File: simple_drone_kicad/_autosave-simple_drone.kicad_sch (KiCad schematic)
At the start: 35 parts, among them P1 USB_C_Plug_USB2.0, Q1 FDN340P, U1 BMI088, U2 BMP581, U3 FT260S-U, U4 LMV358, Y1 Crystal_GND23

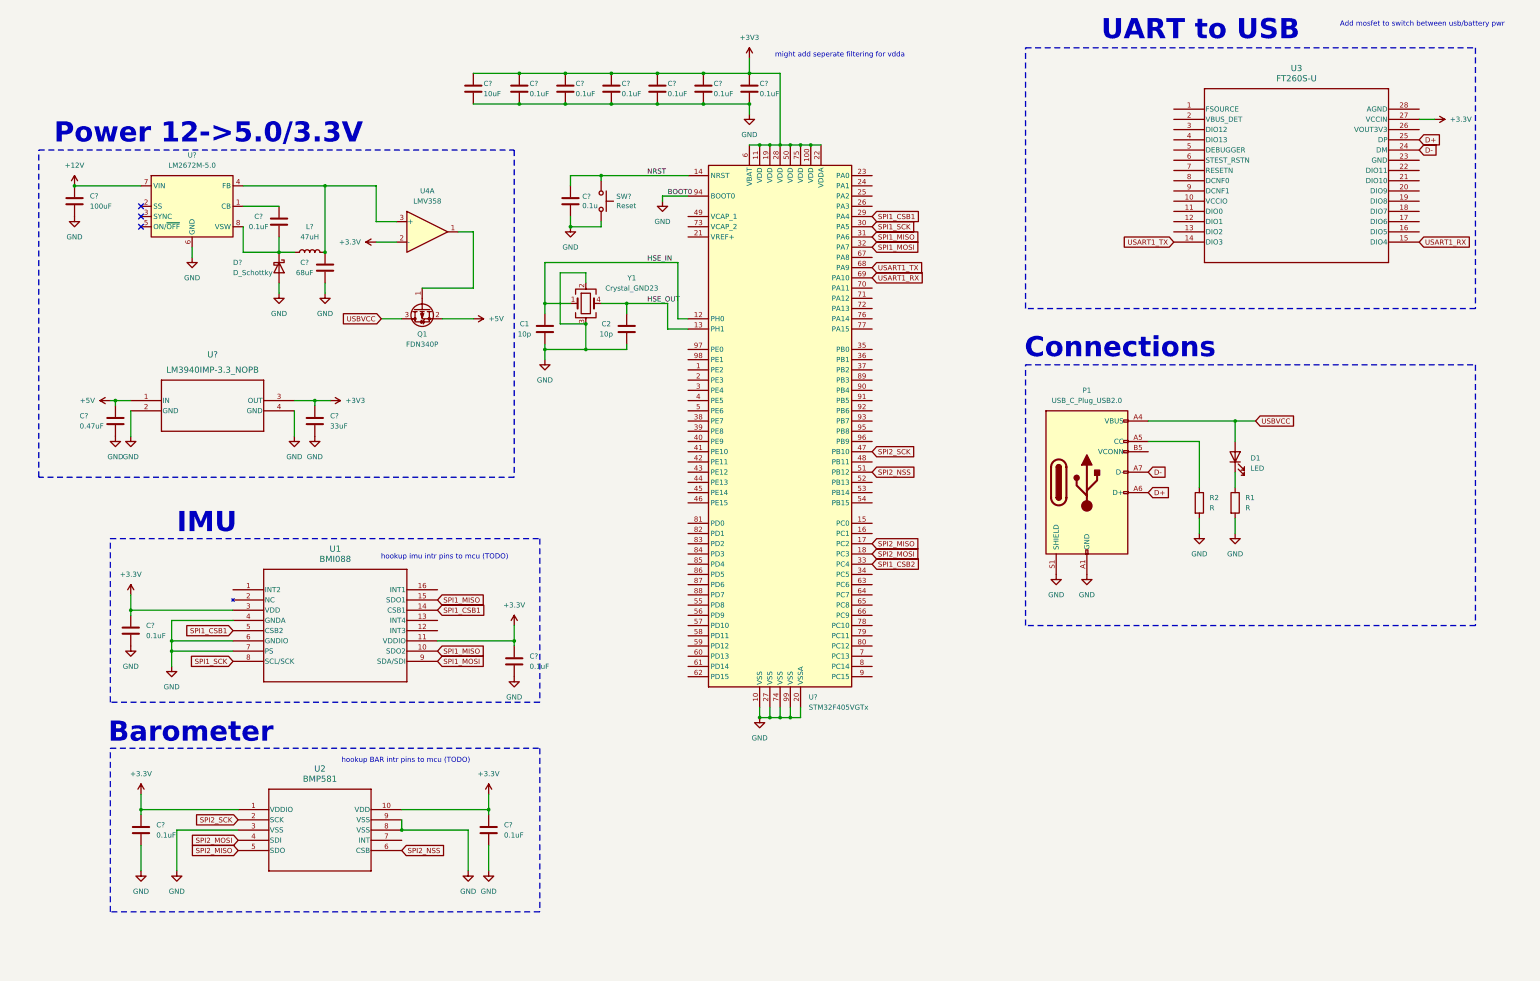
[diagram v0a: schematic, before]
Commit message: added eeprom, fixed power
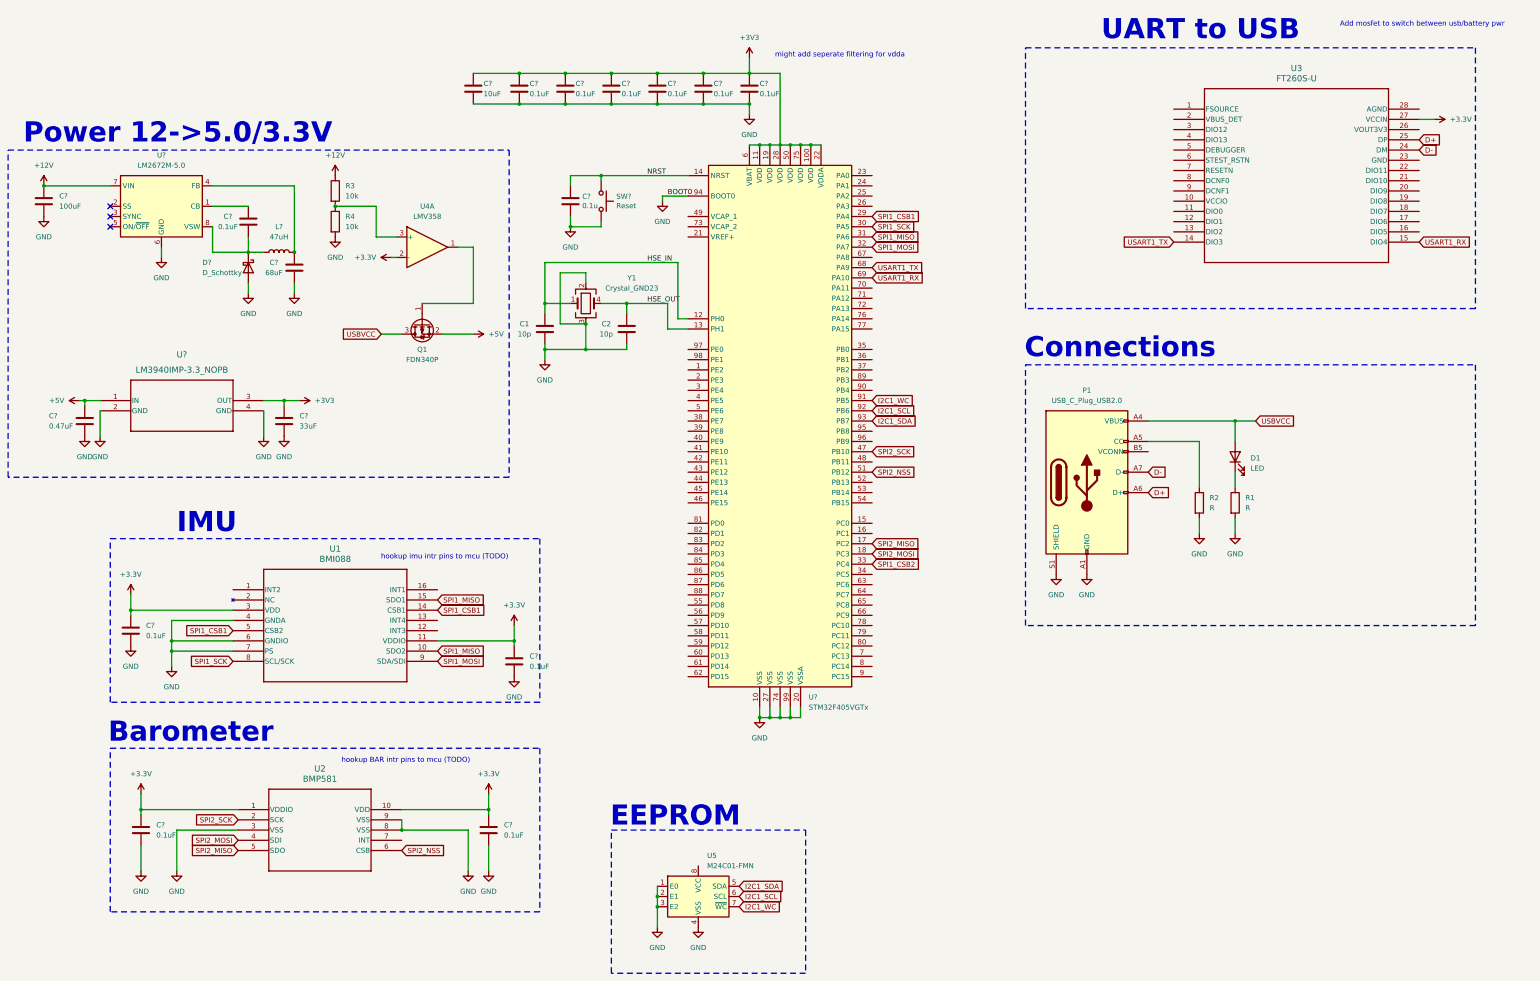
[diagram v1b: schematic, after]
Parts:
- added R3, R4: 10k, symbol Device:R
- added U5: M24C01-FMN, Package_SO:SOIC-8_3.9x4.9mm_P1.27mm, symbol Memory_EEPROM:M24C01-FMN
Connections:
- net +12V: now also R3.1
- net GND: now also R4.2, U5.1 (E0), U5.2 (E1), U5.3 (E2), U5.4 (VSS)
- net at C?.2, L?.2, U?.4 (FB): no longer U4.3 (+)
- net I2C1_WC: now reaches U?.91 (PB5)
- net I2C1_WC: now also U5.7 (~{WC})
- net I2C1_SCL: now reaches U?.92 (PB6)
- net I2C1_SCL: now also U5.6 (SCL)
- net I2C1_SDA: now reaches U?.93 (PB7)
- net I2C1_SDA: now also U5.5 (SDA)
- new net: R3.2, R4.1, U4.3 (+)
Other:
- note added: "EEPROM"
- moved on the sheet: C?, D?, L?, Q1, U4A, U?
